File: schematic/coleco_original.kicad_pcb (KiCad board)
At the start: 2 copper layers, 78.2 x 9.9 mm, 189 parts, among them J0 Conn_01x04, J1 Cartridge Port, J2 Expansion Port, J4A1 Conn_01x08, J4B1 Conn_01x08, J5 DB9_Male, J6 DB9_Male, Q2 2N3906, Q3 2N3906, Q4 2N3904, Q5 2N3904, Q6 2N3906, U1 Z80CPU, U10 MK4116P, U11 MK4116P, U12 MK4116P, U13 MK4116P, U14 MK4116P, U15 MK4116P, U16 MK4116P, U17 MK4116P, U18 74LS541, U19 74LS541, U2 27C256, U20 SN76489AN, U22 74LS04, U23 4066, U24 74LS00, U3 SCM2114AL, U4 SCM2114AL, U5 74LS138, U6 74LS138, U7 74LS05, U8 74LS74, U9 TMS9928A, Y1 7.159090Mhz

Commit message: created edge cut outline for coleco pcb. updated expansion connector edge cut to be the correct size (using a 0.8 mm cutting end in my mill).
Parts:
- added H1: MountingHole_Pad, MountingHole:MountingHole_5.3mm_M5_ISO14580_Pad, F.Cu at (-55.4, 106.4)
- added H2: MountingHole_Pad, MountingHole:MountingHole_5.3mm_M5_ISO14580_Pad, F.Cu at (-35.3, 96.4)
- added H3: MountingHole_Pad, MountingHole:MountingHole_5.3mm_M5_ISO14580_Pad, F.Cu at (-55.4, 96.4)
- added H4: MountingHole_Pad, MountingHole:MountingHole_5.3mm_M5_ISO14580_Pad, F.Cu at (-45.3, 96.4)
- added H5: MountingHole_Pad, MountingHole:MountingHole_5.3mm_M5_ISO14580_Pad, F.Cu at (-45.3, 106.4)
- moved C69 219.8 mm to (360.0, 193.8)
- moved C78 219.8 mm to (347.8, 171.5)
- moved C87 219.8 mm to (342.2, 210.0)
- moved Q6 219.8 mm to (350.6, 198.6)
- moved R18 219.8 mm to (353.0, 176.3)
- moved R41 219.8 mm to (353.0, 180.4)
- moved R48 219.8 mm to (353.0, 184.4)
- moved U23 219.8 mm to (328.7, 186.6)
- moved C62 219.8 mm to (364.0, 180.4)
- moved C66 219.8 mm to (372.5, 168.2)
- moved C67 219.8 mm to (372.5, 164.2)
- moved L15 219.8 mm to (348.2, 165.8)
- moved L8 219.8 mm to (330.4, 207.6)
- moved R40 219.8 mm to (339.9, 196.6)
- moved R42 219.8 mm to (339.9, 200.6)
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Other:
- board size 78.2 x 9.9 mm -> 169.4 x 214.6 mm

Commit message: place a few components for an alignment check. changed edge cut back to 0.1. added new edge.cuts.mill layer for pcb mill edge cuts
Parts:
- moved H3 269.6 mm to (183.4, 221.6)
- moved H4 238.0 mm to (184.4, 34.2)
- moved H5 170.9 mm to (117.1, 159.7)
- moved H1 152.0 mm to (51.3, 214.8)
- moved H2 98.5 mm to (38.4, 30.9)
- moved J1 4.33 mm to (134.6, 170.9)
- moved RF_VL1 0.18 mm to (-56.9, 141.4)
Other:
- board size 169.4 x 214.6 mm -> 168.4 x 213.6 mm

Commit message: first draft of board with components added, no traces
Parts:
- added C11: 100nF, Capacitor_THT:C_Disc_D7.0mm_W2.5mm_P5.00mm, F.Cu at (184.4, 185.6)
- added C16: 10uF, Capacitor_THT:CP_Radial_D5.0mm_P2.50mm, F.Cu at (86.6, 112.0)
- added C2: 100nF, Capacitor_THT:C_Disc_D7.0mm_W2.5mm_P5.00mm, F.Cu at (82.5, 199.8)
- added C21: 100nF, Capacitor_THT:C_Disc_D7.0mm_W2.5mm_P5.00mm, F.Cu at (147.1, 47.9)
- added C22: 100nF, Capacitor_THT:C_Disc_D7.0mm_W2.5mm_P5.00mm, F.Cu at (151.6, 45.1)
- added C23: 100nF, Capacitor_THT:C_Disc_D7.0mm_W2.5mm_P5.00mm, F.Cu at (179.8, 47.7)
- added C24: 100nF, Capacitor_THT:C_Disc_D7.0mm_W2.5mm_P5.00mm, F.Cu at (147.1, 60.4)
- added C26: 100nF, Capacitor_THT:C_Disc_D7.0mm_W2.5mm_P5.00mm, F.Cu at (179.8, 60.1)
- added C27: 100nF, Capacitor_THT:C_Disc_D7.0mm_W2.5mm_P5.00mm, F.Cu at (147.1, 72.8)
- added C28: 100nF, Capacitor_THT:C_Disc_D7.0mm_W2.5mm_P5.00mm, F.Cu at (151.6, 57.6)
- added C29: 100nF, Capacitor_THT:C_Disc_D7.0mm_W2.5mm_P5.00mm, F.Cu at (179.8, 72.6)
- added C30: 100nF, Capacitor_THT:C_Disc_D7.0mm_W2.5mm_P5.00mm, F.Cu at (147.1, 85.2)
- added C31: 100nF, Capacitor_THT:C_Disc_D7.0mm_W2.5mm_P5.00mm, F.Cu at (151.6, 70.0)
- added C32: 100nF, Capacitor_THT:C_Disc_D7.0mm_W2.5mm_P5.00mm, F.Cu at (120.4, 52.4)
- added C36: 10uF, Capacitor_THT:CP_Radial_D5.0mm_P2.50mm, F.Cu at (102.1, 86.5)
- added C37: 100nF, Capacitor_THT:C_Disc_D7.0mm_W2.5mm_P5.00mm, F.Cu at (120.4, 65.1)
- added C40: 100nF, Capacitor_THT:C_Disc_D7.0mm_W2.5mm_P5.00mm, F.Cu at (120.4, 77.6)
- added C42: 100nF, Capacitor_THT:C_Disc_D7.0mm_W2.5mm_P5.00mm, F.Cu at (116.8, 89.8)
- added C43: 100nF, Capacitor_THT:C_Disc_D7.0mm_W2.5mm_P5.00mm, F.Cu at (120.4, 89.8)
- added C44: 100nF, Capacitor_THT:C_Disc_D7.0mm_W2.5mm_P5.00mm, F.Cu at (179.8, 85.0)
- added C45: 100nF, Capacitor_THT:C_Disc_D7.0mm_W2.5mm_P5.00mm, F.Cu at (151.6, 82.5)
- added C60: 47nF, Capacitor_THT:C_Disc_D7.0mm_W2.5mm_P5.00mm, F.Cu at (82.8, 83.7)
- added C7: 100nF, Capacitor_THT:C_Disc_D7.0mm_W2.5mm_P5.00mm, F.Cu at (127.8, 155.1)
- added C8: 100nF, Capacitor_THT:C_Disc_D7.0mm_W2.5mm_P5.00mm, F.Cu at (63.2, 187.1)
- added C89: 100nF, Capacitor_THT:C_Disc_D7.0mm_W2.5mm_P5.00mm, F.Cu at (91.9, 109.9)
- added C9: 100nF, Capacitor_THT:C_Disc_D7.0mm_W2.5mm_P5.00mm, F.Cu at (131.8, 160.1)
- C1, C10, C100, C101, C103, C12, C13, C17, C19, C41, C46, C47, C48, C49, C5, C50, C51, C57, C61, C65, C66, C67, C78, C88, C98, C99: footprint Capacitor_THT:C_Disc_D10.0mm_W2.5mm_P5.00mm -> Capacitor_THT:C_Disc_D7.0mm_W2.5mm_P5.00mm
- C106, C3, C34, C68, C87: footprint Capacitor_THT:CP_Radial_D5.0mm_P2.00mm -> Capacitor_THT:CP_Radial_D5.0mm_P2.50mm
- C69: value 47uF -> 47nF; footprint Capacitor_THT:CP_Radial_D5.0mm_P2.00mm -> Capacitor_THT:C_Disc_D7.0mm_W2.5mm_P5.00mm
- CR1, CR2: footprint Diode_THT:D_DO-35_SOD27_P7.62mm_Horizontal -> Diode_THT:D_DO-35_SOD27_P10.16mm_Horizontal
- JP1, JP2: moved to B.Cu
- L10, L14, L15, L17, L2, L3, L4, L7, L8, L9: footprint Inductor_THT:L_Axial_L12.8mm_D5.8mm_P7.62mm_Vertical_Fastron_HBCC -> Inductor_THT:L_Axial_L11.0mm_D4.5mm_P7.62mm_Vertical_Fastron_MECC
- L5, L6: footprint Inductor_THT:L_Axial_L12.0mm_D5.0mm_P15.24mm_Horizontal_Fastron_MISC -> Inductor_THT:L_Axial_L12.8mm_D5.8mm_P25.40mm_Horizontal_Fastron_HBCC
- R1, R10, R11, R12, R13, R14, R15, R16, R17, R18, R19, R20, R21, R22, R23, R24, R25, R26, R27, R34, R35, R37, R39, R40, R41, R42, R43, R48, R49, R5, R55, R6, R60, R61, R62, R64, R65, R67, R69, R7, R70, R71, R72, R73, R75, R76, R77, R78, R79, R8, R9: footprint Resistor_THT:R_Axial_DIN0207_L6.3mm_D2.5mm_P7.62mm_Horizontal -> Resistor_THT:R_Axial_DIN0207_L6.3mm_D2.5mm_P10.16mm_Horizontal
- RF_JP1, WJ1, WJ2, WJ3, WJ4, WJ5: footprint Resistor_THT:R_Axial_DIN0204_L3.6mm_D1.6mm_P7.62mm_Horizontal -> Resistor_THT:R_Axial_DIN0207_L6.3mm_D2.5mm_P15.24mm_Horizontal
- S1: footprint Button_Switch_THT:SW_TH_Tactile_Omron_B3F-10xx -> Switches_THT:Coleco_RST
- S2: footprint Button_Switch_THT:SW_E-Switch_EG1271_SPDT -> Switches_THT:DPDT_GF-626-0061
- moved JP1 438.7 mm to (103.1, 146.7), turned to -90 degrees
- moved JP2 416.3 mm to (121.2, 143.4), turned to -90 degrees
- moved R14 414.3 mm to (70.1, 208.7)
- moved WJ4 404.9 mm to (102.9, 143.1)
- moved S2 404.5 mm to (33.1, 216.7), turned to 180 degrees
- moved C49 386.4 mm to (54.9, 198.3), turned to -90 degrees
- moved L5 385.4 mm to (44.5, 202.6), turned to 90 degrees
- moved WJ5 381.9 mm to (106.2, 147.5)
- moved L4 378.5 mm to (43.8, 172.1)
- moved R12 377.3 mm to (66.5, 203.6)
- moved U5 377.2 mm to (85.1, 187.1), turned to -90 degrees
- moved U4 373.5 mm to (152.1, 137.0), turned to -90 degrees
- moved C48 372.1 mm to (39.9, 176.7), turned to -90 degrees
- moved J0 368.9 mm to (29.6, 168.4), turned to -90 degrees
- moved U2 366.8 mm to (124.7, 123.8), turned to -90 degrees
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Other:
- board size 168.4 x 213.6 mm -> 168.4 x 213.9 mm

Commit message: added a quick version of the RF board. Not checked at all.
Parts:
- moved RF_C13 81.5 mm to (-78.9, 188.9)
- moved RF_J1 58.0 mm to (-26.4, 150.9), turned to 90 degrees
- moved RF_D1 53.8 mm to (-72.6, 186.1), turned to 90 degrees
- moved RF_C4 53.5 mm to (-63.5, 185.6)
- moved RF_R6 48.2 mm to (-36.8, 155.3), turned to 90 degrees
- moved RF_U1 47.3 mm to (-61.7, 172.6), turned to 90 degrees
- moved RF_R2 46.8 mm to (-68.3, 180.5), turned to 90 degrees
- moved RF_R8 42.2 mm to (-34.5, 183.8)
- moved RF_R3 41.9 mm to (-70.9, 189.9)
- moved RF_R5 41.8 mm to (-35.1, 187.8)
- moved RF_L3 40.6 mm to (-45.2, 189.1)
- moved RF_C10 40.2 mm to (-28.9, 170.6)
- moved RF_D2 36.6 mm to (-65.3, 169.6), turned to 90 degrees
- moved RF_R12 35.4 mm to (-61.0, 158.1)
- moved RF_L2 33.8 mm to (-26.3, 177.9)
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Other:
- board size 168.4 x 213.9 mm -> 281.2 x 213.9 mm

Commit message: fixed RF board placement, not perfect, but needs to align to new component sizes
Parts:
- moved RF_U1 244.6 mm to (125.2, 330.3)
- moved RF_C11 244.2 mm to (163.3, 319.6)
- moved RF_C12 242.6 mm to (143.0, 334.4)
- moved RF_C8 242.6 mm to (143.3, 307.0)
- moved RF_C7 242.6 mm to (137.7, 317.1)
- moved RF_R10 242.1 mm to (124.5, 307.2)
- moved RF_R11 242.1 mm to (123.2, 310.5)
- moved RF_R12 242.1 mm to (124.5, 313.8)
- moved RF_R1 242.1 mm to (103.6, 321.2)
- moved RF_R3 242.1 mm to (117.6, 341.8)
- moved RF_C13 242.0 mm to (108.9, 341.5)
- moved RF_C5 241.9 mm to (123.5, 317.4)
- moved RF_R5 241.9 mm to (150.9, 342.5)
- moved RF_R9 241.8 mm to (138.7, 312.1)
- moved RF_R8 241.3 mm to (150.9, 338.2)
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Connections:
- J4B1 pad 1: GNDD -> (no net)
- J4B1 pad 2: /rf_mod/sub_rf_mod/2 -> (no net)
- J4B1 pad 3: /rf_mod/sub_rf_mod/3 -> (no net)
- J4B1 pad 4: VDDF -> (no net)
- J4B1 pad 5: /rf_mod/sub_rf_mod/5 -> (no net)
- J4B1 pad 6: /rf_mod/sub_rf_mod/6 -> (no net)
- J4B1 pad 7: /rf_mod/sub_rf_mod/7 -> (no net)
- J4B1 pad 8: /rf_mod/sub_rf_mod/8 -> (no net)
- RF_C1 pad 1: Net-(RF_C1-Pad1) -> (no net)
- RF_C1 pad 2: GNDD -> (no net)
- RF_C10 pad 1: Net-(RF_C10-Pad1) -> (no net)
- RF_C10 pad 2: Net-(RF_C10-Pad2) -> (no net)
- RF_C11 pad 1: Net-(RF_C11-Pad1) -> (no net)
- RF_C11 pad 2: GNDD -> (no net)
- RF_C12 pad 1: Net-(RF_C12-Pad1) -> (no net)
- RF_C12 pad 2: Net-(RF_C12-Pad2) -> (no net)
- RF_C13 pad 1: VDDF -> (no net)
- RF_C13 pad 2: GNDD -> (no net)
- RF_C2 pad 1: GNDD -> (no net)
- RF_C2 pad 2: /rf_mod/sub_rf_mod/2 -> (no net)
- RF_C3 pad 1: Net-(RF_C3-Pad1) -> (no net)
- RF_C3 pad 2: Net-(RF_C3-Pad2) -> (no net)
- RF_C4 pad 1: Net-(RF_C3-Pad2) -> (no net)
- RF_C4 pad 2: /rf_mod/sub_rf_mod/8 -> (no net)
- RF_C5 pad 1: Net-(RF_C5-Pad1) -> (no net)
- RF_C5 pad 2: /rf_mod/sub_rf_mod/5 -> (no net)
- RF_C6 pad 1: Net-(RF_C6-Pad1) -> (no net)
- RF_C6 pad 2: Net-(RF_C12-Pad2) -> (no net)
- RF_C7 pad 1: Net-(RF_C7-Pad1) -> (no net)
- RF_C7 pad 2: Net-(RF_C7-Pad2) -> (no net)
- RF_C8 pad 1: Net-(RF_C1-Pad1) -> (no net)
- RF_C8 pad 2: GNDD -> (no net)
- RF_C9 pad 1: Net-(RF_C10-Pad2) -> (no net)
- RF_C9 pad 2: GNDD -> (no net)
- RF_D1 pad 1: VDDF -> (no net)
- RF_D1 pad 2: /rf_mod/sub_rf_mod/5 -> (no net)
- RF_D2 pad 1: Net-(RF_D2-Pad1) -> (no net)
- RF_D2 pad 2: /rf_mod/sub_rf_mod/2 -> (no net)
- RF_JP1 pad 1: Net-(RF_C1-Pad1) -> (no net)
- RF_JP1 pad 2: VDDF -> (no net)
- RF_L1 pad 1: Net-(RF_C10-Pad2) -> (no net)
- RF_L1 pad 2: Net-(RF_C11-Pad1) -> (no net)
- RF_L2 pad 1: Net-(RF_L2-Pad1) -> (no net)
- RF_L2 pad 2: Net-(RF_C10-Pad1) -> (no net)
- RF_L3 pad 1: Net-(RF_C6-Pad1) -> (no net)
- RF_L3 pad 2: Net-(RF_C12-Pad2) -> (no net)
- RF_R1 pad 1: /rf_mod/sub_rf_mod/5 -> (no net)
- RF_R1 pad 2: /rf_mod/sub_rf_mod/2 -> (no net)
- RF_R10 pad 1: VDDF -> (no net)
- RF_R10 pad 2: /rf_mod/sub_rf_mod/2 -> (no net)
- RF_R11 pad 1: Net-(RF_C7-Pad2) -> (no net)
- RF_R11 pad 2: /rf_mod/sub_rf_mod/5 -> (no net)
- RF_R12 pad 1: Net-(RF_C7-Pad1) -> (no net)
- RF_R12 pad 2: Net-(RF_D2-Pad1) -> (no net)
- RF_R2 pad 1: Net-(RF_C5-Pad1) -> (no net)
- RF_R2 pad 2: /rf_mod/sub_rf_mod/8 -> (no net)
- RF_R3 pad 1: GNDD -> (no net)
- RF_R3 pad 2: Net-(RF_C3-Pad2) -> (no net)
- RF_R4 pad 1: GNDD -> (no net)
- RF_R4 pad 2: /rf_mod/sub_rf_mod/5 -> (no net)
- RF_R5 pad 1: VDDF -> (no net)
- RF_R5 pad 2: Net-(RF_C6-Pad1) -> (no net)
- RF_R6 pad 1: Net-(RF_C12-Pad2) -> (no net)
- RF_R6 pad 2: VDDF -> (no net)
- RF_R7 pad 1: Net-(RF_C10-Pad2) -> (no net)
- RF_R7 pad 2: GNDD -> (no net)
- RF_R8 pad 1: Net-(RF_L2-Pad1) -> (no net)
- RF_R8 pad 2: Net-(RF_C1-Pad1) -> (no net)
- RF_R9 pad 1: Net-(RF_C7-Pad2) -> (no net)
- RF_R9 pad 2: Net-(RF_C1-Pad1) -> (no net)
- RF_SW1 pad 1: Net-(RF_C6-Pad1) -> (no net)
- RF_SW1 pad 2: Net-(RF_C12-Pad1) -> (no net)
- RF_SW1 pad 3: unconnected-(RF_SW1-Pad3) -> (no net)
- RF_U1 pad 1: Net-(RF_C3-Pad1) -> (no net)
- RF_U1 pad 10: Net-(RF_L2-Pad1) -> (no net)
- RF_U1 pad 11: unconnected-(RF_U1-Pad11) -> (no net)
- RF_U1 pad 12: Net-(RF_C7-Pad2) -> (no net)
- RF_U1 pad 13: /rf_mod/sub_rf_mod/6 -> (no net)
- RF_U1 pad 14: Net-(RF_C1-Pad1) -> (no net)
- RF_U1 pad 15: Net-(RF_D2-Pad1) -> (no net)
- RF_U1 pad 16: Net-(RF_C1-Pad1) -> (no net)
- RF_U1 pad 17: unconnected-(RF_U1-Pad17) -> (no net)
- RF_U1 pad 18: Net-(RF_C5-Pad1) -> (no net)
- RF_U1 pad 2: /rf_mod/sub_rf_mod/3 -> (no net)
- RF_U1 pad 3: /rf_mod/sub_rf_mod/5 -> (no net)
- RF_U1 pad 4: /rf_mod/sub_rf_mod/7 -> (no net)
- RF_U1 pad 5: GNDD -> (no net)
- RF_U1 pad 6: Net-(RF_C12-Pad2) -> (no net)
- RF_U1 pad 7: Net-(RF_C6-Pad1) -> (no net)
- RF_U1 pad 8: unconnected-(RF_U1-Pad8) -> (no net)
- RF_U1 pad 9: unconnected-(RF_U1-Pad9) -> (no net)
- RF_VL1 pad 1: Net-(RF_C1-Pad1) -> (no net)
- RF_VL1 pad 2: unconnected-(RF_VL1-Pad2) -> (no net)
- RF_VL1 pad 3: Net-(RF_D2-Pad1) -> (no net)
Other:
- board size 281.2 x 213.9 mm -> 168.4 x 318 mm

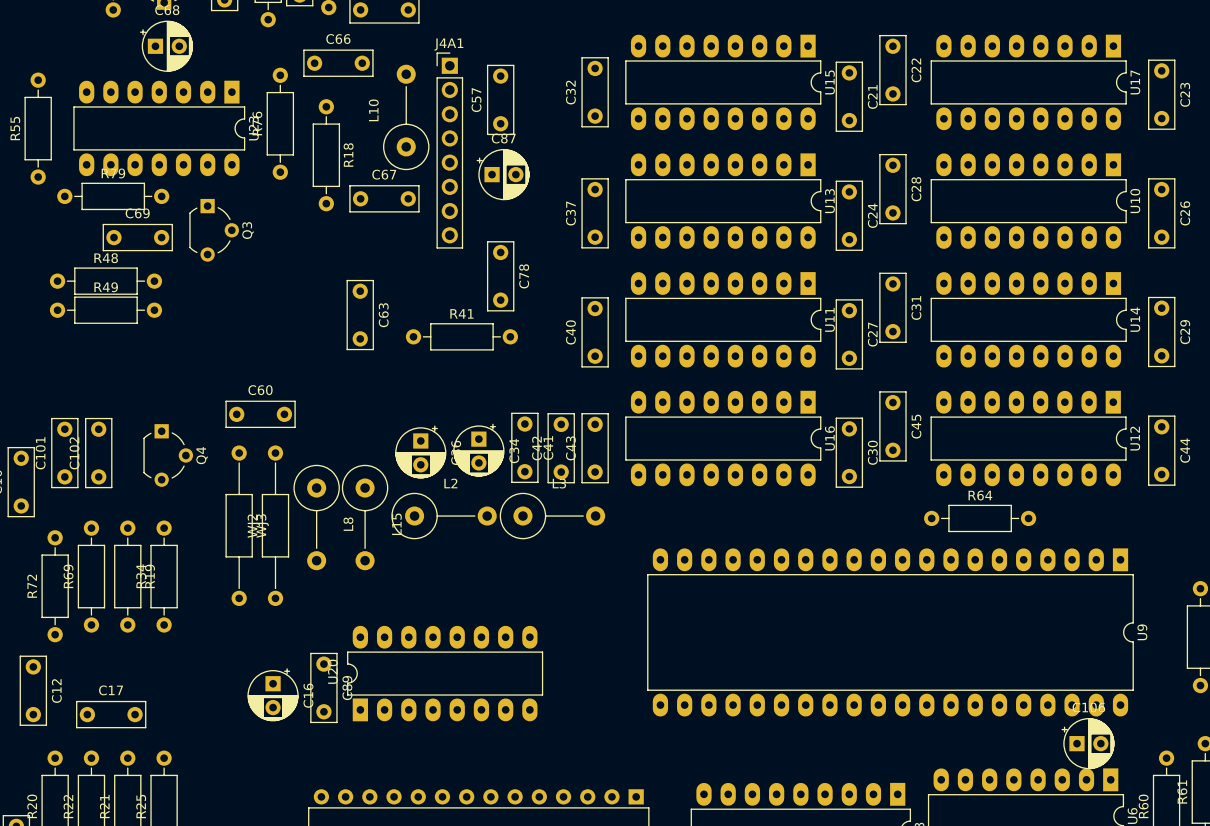
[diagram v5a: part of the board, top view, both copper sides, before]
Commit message: RF on main board components setup correctly.
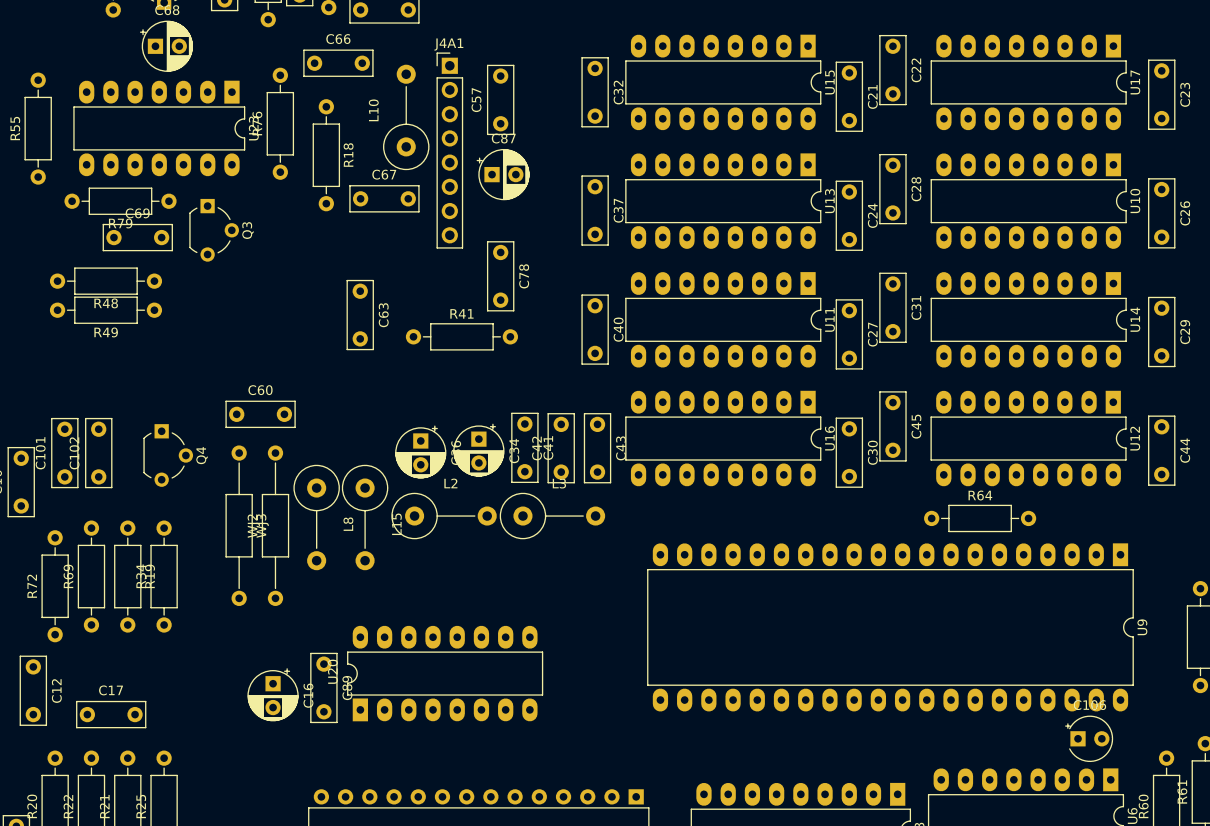
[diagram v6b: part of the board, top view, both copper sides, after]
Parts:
- C106: footprint Capacitor_THT:CP_Radial_D5.0mm_P2.50mm -> Capacitor_THT:CP_Radial_Tantal_D4.5mm_P2.50mm
- moved R79 10.9 mm to (104.6, 71.5), turned to 180 degrees
- moved R48 10.2 mm to (103.1, 79.9), turned to 180 degrees
- moved R49 10.2 mm to (103.1, 82.9), turned to 180 degrees
- moved C40 5.29 mm to (149.4, 82.5), turned to -90 degrees
- moved C37 5.29 mm to (149.4, 70.0), turned to -90 degrees
- moved C43 5.01 mm to (149.6, 94.9), turned to -90 degrees
- moved C32 5.00 mm to (149.4, 57.6), turned to -90 degrees
- moved U9 0.53 mm to (204.5, 108.6)
- moved C106 0.52 mm to (200.0, 127.9)
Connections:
- J4B1 pad 1: (no net) -> GNDD
- J4B1 pad 2: (no net) -> /rf_mod/sub_rf_mod/2
- J4B1 pad 3: (no net) -> /rf_mod/sub_rf_mod/3
- J4B1 pad 4: (no net) -> VDDF
- J4B1 pad 5: (no net) -> /rf_mod/sub_rf_mod/5
- J4B1 pad 6: (no net) -> /rf_mod/sub_rf_mod/6
- J4B1 pad 7: (no net) -> /rf_mod/sub_rf_mod/7
- J4B1 pad 8: (no net) -> /rf_mod/sub_rf_mod/8
- RF_C1 pad 1: (no net) -> Net-(RF_C1-Pad1)
- RF_C1 pad 2: (no net) -> GNDD
- RF_C10 pad 1: (no net) -> Net-(RF_C10-Pad1)
- RF_C10 pad 2: (no net) -> Net-(RF_C10-Pad2)
- RF_C11 pad 1: (no net) -> Net-(RF_C11-Pad1)
- RF_C11 pad 2: (no net) -> GNDD
- RF_C12 pad 1: (no net) -> Net-(RF_C12-Pad1)
- RF_C12 pad 2: (no net) -> Net-(RF_C12-Pad2)
- RF_C13 pad 1: (no net) -> VDDF
- RF_C13 pad 2: (no net) -> GNDD
- RF_C2 pad 1: (no net) -> GNDD
- RF_C2 pad 2: (no net) -> /rf_mod/sub_rf_mod/2
- RF_C3 pad 1: (no net) -> Net-(RF_C3-Pad1)
- RF_C3 pad 2: (no net) -> Net-(RF_C3-Pad2)
- RF_C4 pad 1: (no net) -> Net-(RF_C3-Pad2)
- RF_C4 pad 2: (no net) -> /rf_mod/sub_rf_mod/8
- RF_C5 pad 1: (no net) -> Net-(RF_C5-Pad1)
- RF_C5 pad 2: (no net) -> /rf_mod/sub_rf_mod/5
- RF_C6 pad 1: (no net) -> Net-(RF_C6-Pad1)
- RF_C6 pad 2: (no net) -> Net-(RF_C12-Pad2)
- RF_C7 pad 1: (no net) -> Net-(RF_C7-Pad1)
- RF_C7 pad 2: (no net) -> Net-(RF_C7-Pad2)
- RF_C8 pad 1: (no net) -> Net-(RF_C1-Pad1)
- RF_C8 pad 2: (no net) -> GNDD
- RF_C9 pad 1: (no net) -> Net-(RF_C10-Pad2)
- RF_C9 pad 2: (no net) -> GNDD
- RF_D1 pad 1: (no net) -> VDDF
- RF_D1 pad 2: (no net) -> /rf_mod/sub_rf_mod/5
- RF_D2 pad 1: (no net) -> Net-(RF_D2-Pad1)
- RF_D2 pad 2: (no net) -> /rf_mod/sub_rf_mod/2
- RF_JP1 pad 1: (no net) -> Net-(RF_C1-Pad1)
- RF_JP1 pad 2: (no net) -> VDDF
- RF_L1 pad 1: (no net) -> Net-(RF_C10-Pad2)
- RF_L1 pad 2: (no net) -> Net-(RF_C11-Pad1)
- RF_L2 pad 1: (no net) -> Net-(RF_L2-Pad1)
- RF_L2 pad 2: (no net) -> Net-(RF_C10-Pad1)
- RF_L3 pad 1: (no net) -> Net-(RF_C6-Pad1)
- RF_L3 pad 2: (no net) -> Net-(RF_C12-Pad2)
- RF_R1 pad 1: (no net) -> /rf_mod/sub_rf_mod/5
- RF_R1 pad 2: (no net) -> /rf_mod/sub_rf_mod/2
- RF_R10 pad 1: (no net) -> VDDF
- RF_R10 pad 2: (no net) -> /rf_mod/sub_rf_mod/2
- RF_R11 pad 1: (no net) -> Net-(RF_C7-Pad2)
- RF_R11 pad 2: (no net) -> /rf_mod/sub_rf_mod/5
- RF_R12 pad 1: (no net) -> Net-(RF_C7-Pad1)
- RF_R12 pad 2: (no net) -> Net-(RF_D2-Pad1)
- RF_R2 pad 1: (no net) -> Net-(RF_C5-Pad1)
- RF_R2 pad 2: (no net) -> /rf_mod/sub_rf_mod/8
- RF_R3 pad 1: (no net) -> GNDD
- RF_R3 pad 2: (no net) -> Net-(RF_C3-Pad2)
- RF_R4 pad 1: (no net) -> GNDD
- RF_R4 pad 2: (no net) -> /rf_mod/sub_rf_mod/5
- RF_R5 pad 1: (no net) -> VDDF
- RF_R5 pad 2: (no net) -> Net-(RF_C6-Pad1)
- RF_R6 pad 1: (no net) -> Net-(RF_C12-Pad2)
- RF_R6 pad 2: (no net) -> VDDF
- RF_R7 pad 1: (no net) -> Net-(RF_C10-Pad2)
- RF_R7 pad 2: (no net) -> GNDD
- RF_R8 pad 1: (no net) -> Net-(RF_L2-Pad1)
- RF_R8 pad 2: (no net) -> Net-(RF_C1-Pad1)
- RF_R9 pad 1: (no net) -> Net-(RF_C7-Pad2)
- RF_R9 pad 2: (no net) -> Net-(RF_C1-Pad1)
- RF_SW1 pad 1: (no net) -> Net-(RF_C6-Pad1)
- RF_SW1 pad 2: (no net) -> Net-(RF_C12-Pad1)
- RF_SW1 pad 3: (no net) -> unconnected-(RF_SW1-Pad3)
- RF_U1 pad 1: (no net) -> Net-(RF_C3-Pad1)
- RF_U1 pad 10: (no net) -> Net-(RF_L2-Pad1)
- RF_U1 pad 11: (no net) -> unconnected-(RF_U1-Pad11)
- RF_U1 pad 12: (no net) -> Net-(RF_C7-Pad2)
- RF_U1 pad 13: (no net) -> /rf_mod/sub_rf_mod/6
- RF_U1 pad 14: (no net) -> Net-(RF_C1-Pad1)
- RF_U1 pad 15: (no net) -> Net-(RF_D2-Pad1)
- RF_U1 pad 16: (no net) -> Net-(RF_C1-Pad1)
- RF_U1 pad 17: (no net) -> unconnected-(RF_U1-Pad17)
- RF_U1 pad 18: (no net) -> Net-(RF_C5-Pad1)
- RF_U1 pad 2: (no net) -> /rf_mod/sub_rf_mod/3
- RF_U1 pad 3: (no net) -> /rf_mod/sub_rf_mod/5
- RF_U1 pad 4: (no net) -> /rf_mod/sub_rf_mod/7
- RF_U1 pad 5: (no net) -> GNDD
- RF_U1 pad 6: (no net) -> Net-(RF_C12-Pad2)
- RF_U1 pad 7: (no net) -> Net-(RF_C6-Pad1)
- RF_U1 pad 8: (no net) -> unconnected-(RF_U1-Pad8)
- RF_U1 pad 9: (no net) -> unconnected-(RF_U1-Pad9)
- RF_VL1 pad 1: (no net) -> Net-(RF_C1-Pad1)
- RF_VL1 pad 2: (no net) -> unconnected-(RF_VL1-Pad2)
- RF_VL1 pad 3: (no net) -> Net-(RF_D2-Pad1)
